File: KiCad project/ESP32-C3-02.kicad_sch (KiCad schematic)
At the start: 27 parts, among them J3 GSD090012SEU, U3 ESP32-C3-WROOM-02-H4, U4 CP2102N-A02-GQFN20, U5 USBLC6-2SC6, U6 W25Q32JVSSIQ

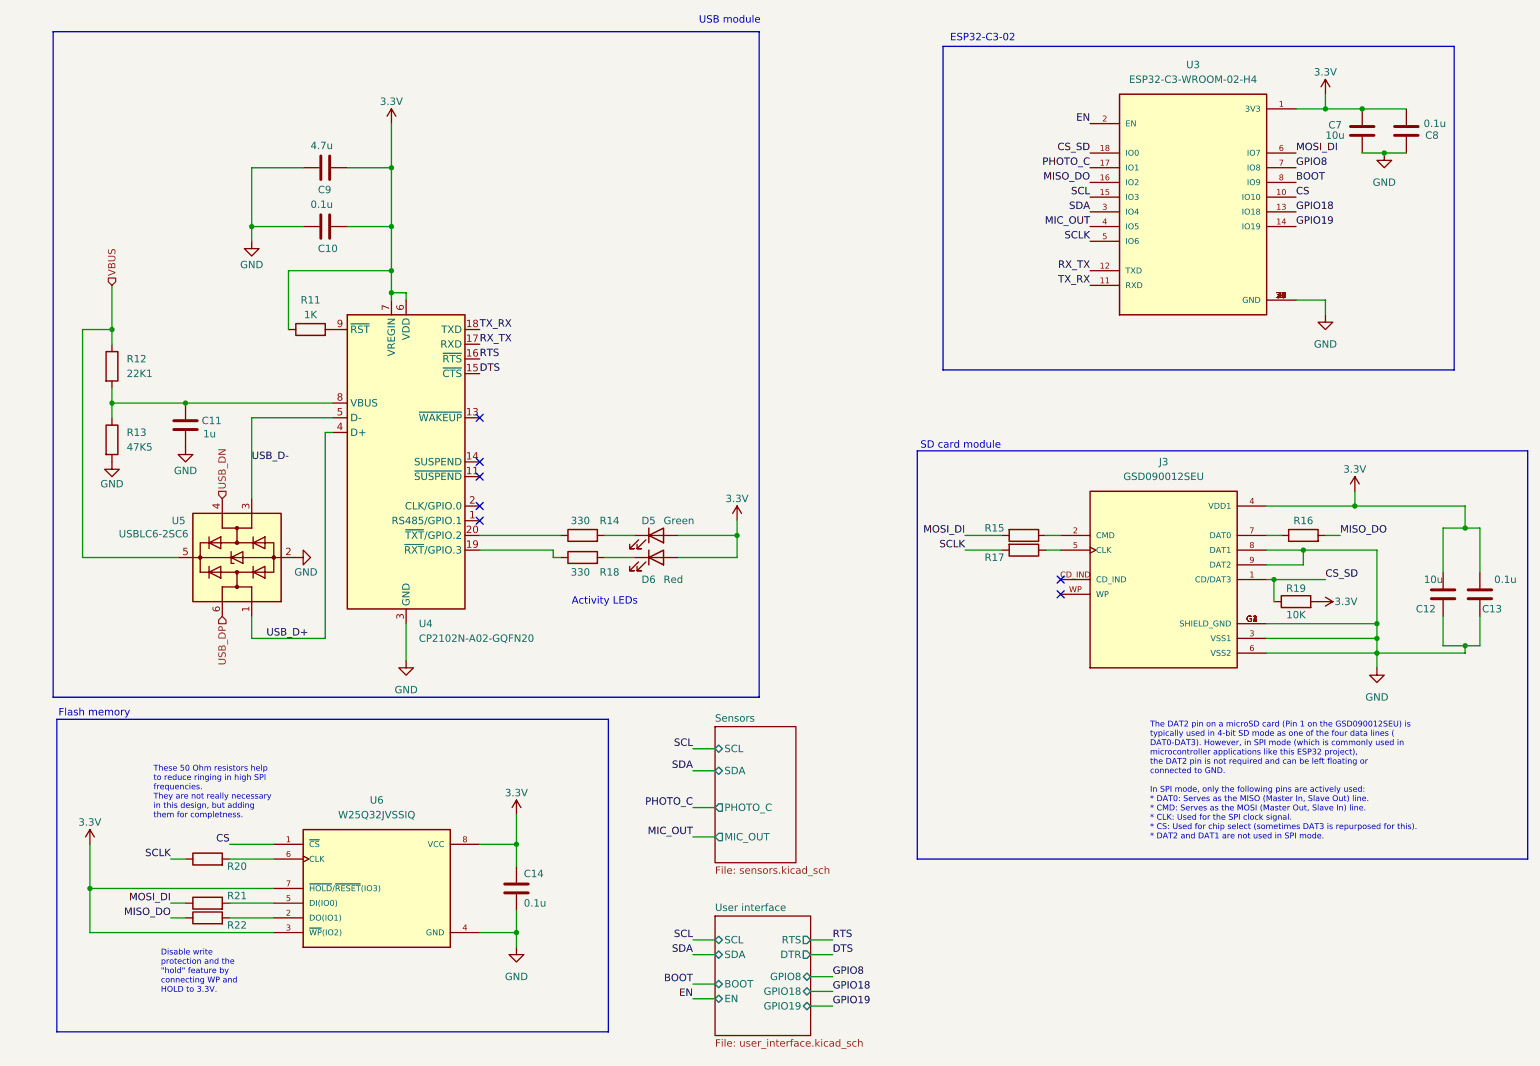
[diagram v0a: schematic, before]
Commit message: Replaced the button, USB, bat connector with new symbols and footprints. Completed draft layout and routing.
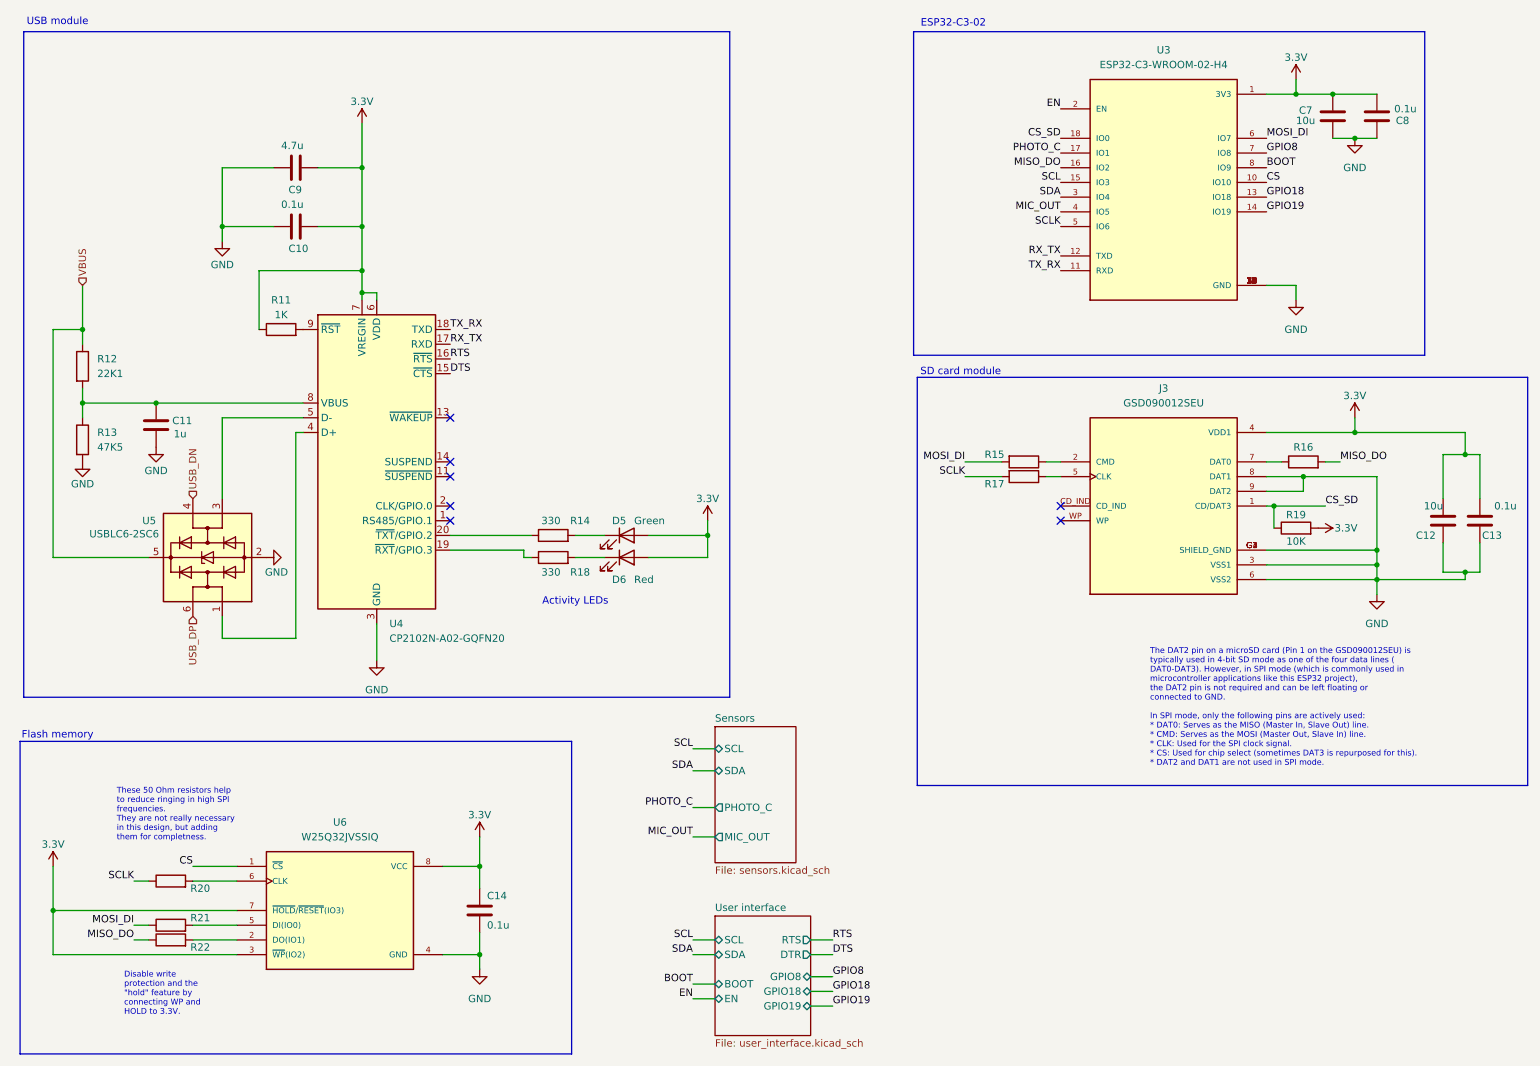
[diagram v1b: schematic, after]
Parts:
- J3: Manufacturer_Part_Number (none) -> GSD090012SEU
- R11, R12, R13, R14, R15, R16, R17, R18, R19, R20, R21, R22: PACKAGE (none) -> 0805
- U3: footprint Project_Library:MODULE_ESP32-C3-WROOM-02-H4 -> Footprints:MODULE_ESP32-C3-WROOM-02-H4; MANUFACTURER (none) -> Espressif; Manufacturer_Part_Number (none) -> ESP32-C3-WROOM-02-H4
- U4: MANUFACTURER (none) -> Silicon Laboratories; Manufacturer_Part_Number (none) -> CP2102N-A02-GQFN20; PACKAGE (none) -> QFN20
- U5: MANUFACTURER (none) -> STMicroelectronics; PACKAGE (none) -> SOT-23-6
- U6: MANUFACTURER (none) -> Winbond; Manufacturer_Part_Number (none) -> W25Q32JVSSIQ; PACKAGE (none) -> SOIC-8
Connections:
- net USB_D+: no longer names the net of U4.4 (D+), U5.1 (I/O1)
- net USB_D-: no longer names the net of U4.5 (D-), U5.3 (I/O2)
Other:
- moved on the sheet: C10, C11, C12, C13, C14, C7, C8, C9, D5, D6, J3, R11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

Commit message: Replaced tantalum capacitors and LEDs.
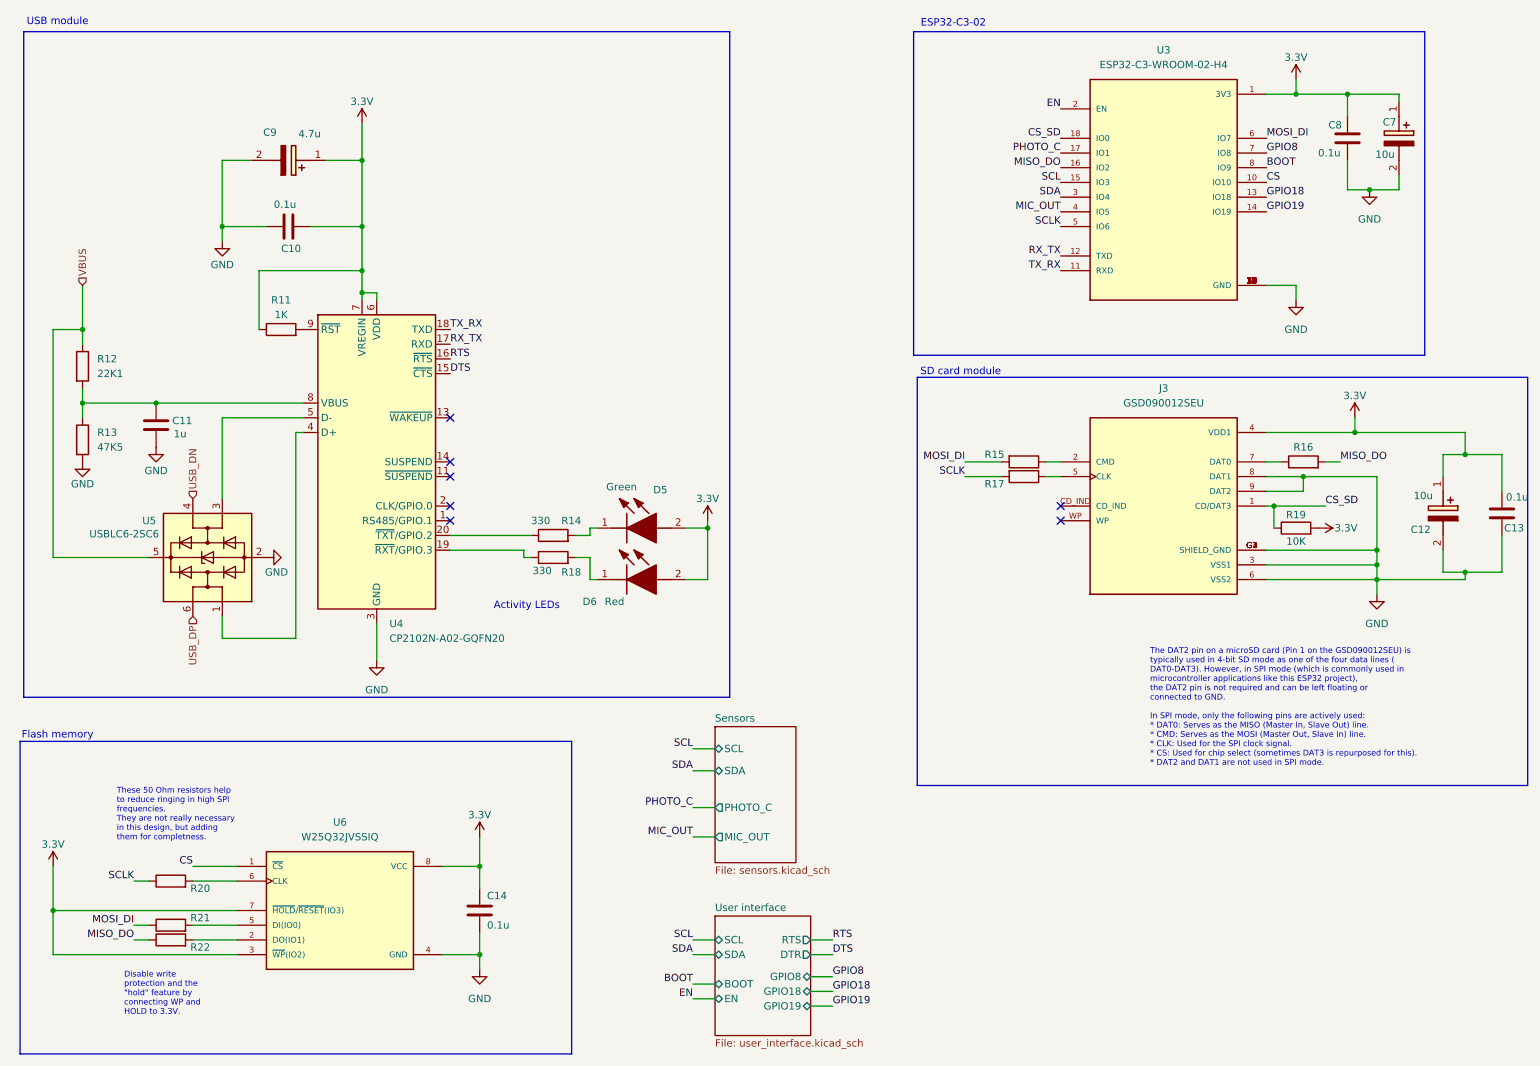
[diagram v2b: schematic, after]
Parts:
- C12: footprint Capacitor_SMD:C_0805_2012Metric -> T491A; symbol SparkFun-Capacitor:C -> T491A106K010AT7280:T491A106K010AT7280; Arrow Part Number (none) -> T491A106K010AT7280; Arrow Price/Stock (none) -> https://www.arrow.com/en/products/t491a106k010at7280/kemet-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; Comments (none) -> Download this part from https://componentsearchengine.com/p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; Height (none) -> 1.8; Manufacturer_Name (none) -> KEMET; Manufacturer_Part_Number (none) -> T491A106K010AT7280; Mouser Part Number (none) -> 80-T491A106K107280; Mouser Price/Stock (none) -> https://www.mouser.co.uk/ProductDetail/KEMET/T491A106K010AT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
- C7: renamed from C8; value 0.1u -> 10u; footprint Capacitor_SMD:C_0805_2012Metric -> T491A; symbol SparkFun-Capacitor:C -> T491A106K010AT7280:T491A106K010AT7280; Arrow Part Number (none) -> T491A106K010AT7280; Arrow Price/Stock (none) -> https://www.arrow.com/en/products/t491a106k010at7280/kemet-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; Height (none) -> 1.8; Manufacturer_Name (none) -> KEMET; Manufacturer_Part_Number (none) -> T491A106K010AT7280; Mouser Part Number (none) -> 80-T491A106K107280; Mouser Price/Stock (none) -> https://www.mouser.co.uk/ProductDetail/KEMET/T491A106K010AT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
- C8: renamed from C7; value 10u -> 0.1u; Instructions and notes (none) -> Download this part from https://componentsearchengine.com/p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
- C9: footprint Capacitor_SMD:C_0805_2012Metric -> T491A; symbol SparkFun-Capacitor:C -> T491A106K010AT7280:T491A106K010AT7280; Arrow Part Number (none) -> T491A106K010AT7280; Arrow Price/Stock (none) -> https://www.arrow.com/en/products/t491a106k010at7280/kemet-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; Height (none) -> 1.8; Instructions and notes (none) -> Download from https://componentsearchengine.com/part-view/T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; Manufacturer_Name (none) -> KEMET; Manufacturer_Part_Number (none) -> T491A106K010AT7280; Mouser Part Number (none) -> 80-T491A106K107280; Mouser Price/Stock (none) -> https://www.mouser.co.uk/ProductDetail/KEMET/T491A106K010AT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
- D5: footprint LED_SMD:LED_0603_1608Metric -> LEDC2012X120N; symbol SparkFun-LED:LED_Green_0603 -> LTST-C170GKT:LTST-C170GKT; Arrow Part Number (none) -> LTST-C170GKT; Arrow Price/Stock (none) -> https://www.arrow.com/en/products/ltst-c170gkt/lite-on-tech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; Comments (none) -> Download from https://componentsearchengine.com/part-view/L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; Height (none) -> 1.2; Manufacturer_Name (none) -> Lite-On; Manufacturer_Part_Number (none) -> LTST-C170GKT; Mouser Part Number (none) -> 859-LTST-C170GKT; Mouser Price/Stock (none) -> https://www.mouser.co.uk/ProductDetail/Lite-On/LTST-C170GKT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
- D6: footprint LED_SMD:LED_0603_1608Metric -> LEDC2012X120N; symbol SparkFun-LED:LED_Red_0603 -> LTST-C170KRKT:LTST-C170KRKT; Arrow Part Number (none) -> LTST-C170KRKT; Arrow Price/Stock (none) -> https://www.arrow.com/en/products/ltst-c170krkt/lite-on-tec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; Height (none) -> 1.2; Manufacturer_Name (none) -> Lite-On; Manufacturer_Part_Number (none) -> LTST-C170KRKT; Mouser Part Number (none) -> 859-LTST-C170KRKT; Mouser Price/Stock (none) -> https://www.mouser.co.uk/ProductDetail/Lite-On/LTST-C170KRK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
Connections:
- net 3.3V: now also C12.1 (+), C7.1 (+); no longer C12.2, C7.2
- net GND: now also C12.2 (-), C7.2 (-); no longer C12.1, C7.1
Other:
- moved on the sheet: C10, C13, C8

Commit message: Layout in progress.
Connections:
- net USB_D+: now reaches U4.4 (D+), U5.1 (I/O1)
- net USB_D-: now reaches U4.5 (D-), U5.3 (I/O2)
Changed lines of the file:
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@@
+		)
+	)
+	(label "USB_D+"
+		(at 55.88 120.65 0)
+		(fields_autoplaced yes)
+		(effects
+			(font
+				(size 1.27 1.27)
+			)
+			(justify left bottom)
 		)
 	)
@@
 		)
 	)
+	(label "USB_D-"
+		(at 53.34 87.63 0)
+		(fields_autoplaced yes)
+		(effects
+			(font
+				(size 1.27 1.27)
+			)
+			(justify left bottom)
+		)
+	)
